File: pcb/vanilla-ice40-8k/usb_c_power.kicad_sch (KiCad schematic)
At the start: 25 parts, among them J8 Conn_01x02_Pin, U5 TPS563252DRLR, U6 TPS563252DRLR

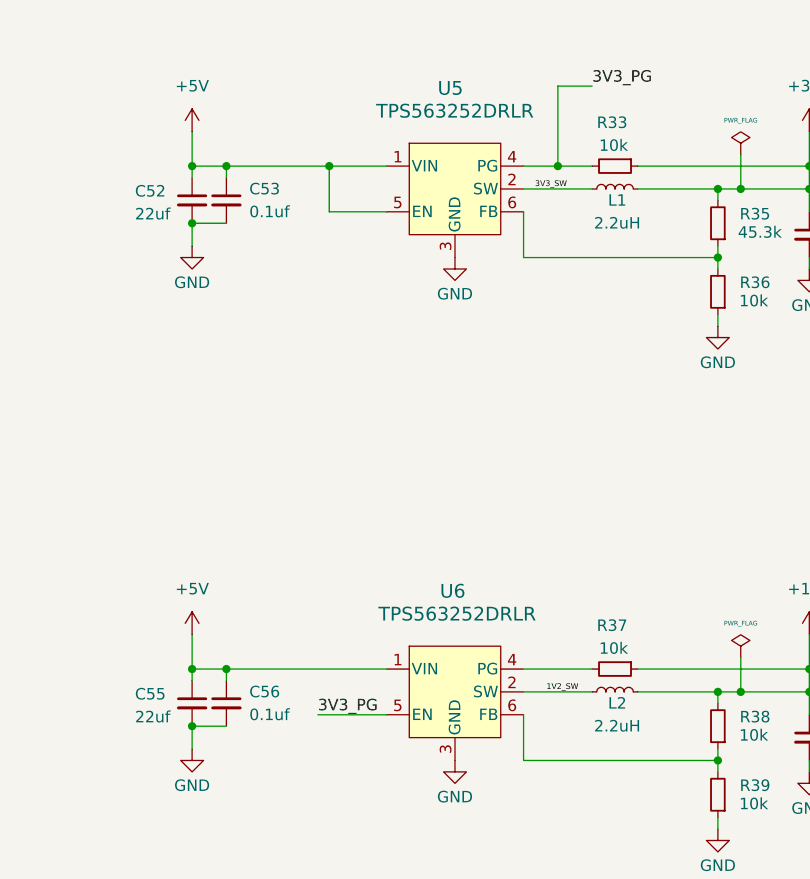
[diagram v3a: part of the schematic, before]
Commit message: [hx8k][pcb] rough layout of full board
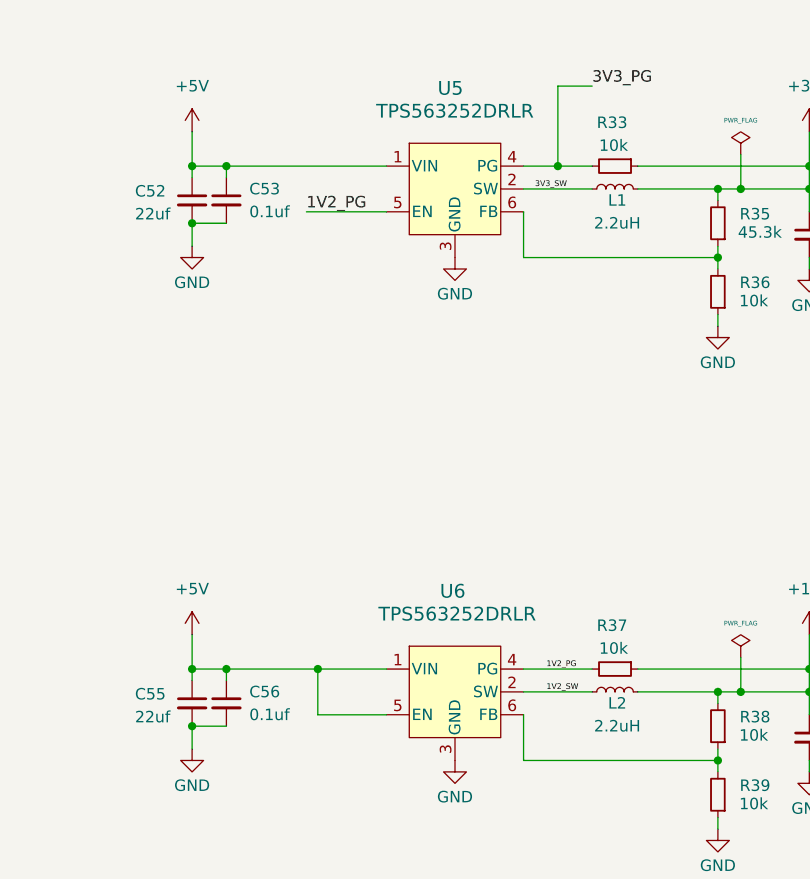
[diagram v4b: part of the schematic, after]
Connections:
- net +5V: now also U6.5 (EN); no longer U5.5 (EN)
- net 3V3_PG: no longer U6.5 (EN)
- net 1V2_PG: now reaches R37.2, U6.4 (PG)
- net 1V2_PG: now also U5.5 (EN)
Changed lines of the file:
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@@
-	)
-	(junction
-		(at 139.7 67.31)
-		(diameter 0)
-		(color 0 0 0 0)
 	)
 	(junction
@@
 	(junction
 		(at 124.46 67.31)
+		(diameter 0)
+		(color 0 0 0 0)
+	)
+	(junction
+		(at 138.43 123.19)
 		(diameter 0)
 		(color 0 0 0 0)
@@
 	(wire
 		(pts
-			(xy 139.7 67.31) (xy 139.7 72.39)
-		)
-		(stroke
-			(width 0)
-			(type default)
-		)
-	)
-	(wire
-		(pts
 			(xy 124.46 129.54) (xy 124.46 132.08)
 		)
@@
 	(wire
 		(pts
-			(xy 128.27 123.19) (xy 146.05 123.19)
+			(xy 128.27 123.19) (xy 138.43 123.19)
 		)
 		(stroke
@@
 	(wire
 		(pts
-			(xy 128.27 67.31) (xy 139.7 67.31)
+			(xy 128.27 67.31) (xy 146.05 67.31)
 		)
 		(stroke
@@
 	(wire
 		(pts
-			(xy 139.7 67.31) (xy 146.05 67.31)
-		)
-		(stroke
-			(width 0)
-			(type default)
-		)
-	)
-	(wire
-		(pts
 			(xy 43.18 31.75) (xy 43.18 34.29)
 		)
@@
 	(wire
 		(pts
+			(xy 138.43 123.19) (xy 146.05 123.19)
+		)
+		(stroke
+			(width 0)
+			(type default)
+		)
+	)
+	(wire
+		(pts
 			(xy 165.1 67.31) (xy 165.1 58.42)
 		)
@@
 	(wire
 		(pts
+			(xy 138.43 123.19) (xy 138.43 128.27)
+		)
+		(stroke
+			(width 0)
+			(type default)
+		)
+	)
+	(wire
+		(pts
 			(xy 182.88 69.85) (xy 185.42 69.85)
 		)
@@
 	(wire
 		(pts
-			(xy 139.7 72.39) (xy 146.05 72.39)
+			(xy 137.16 72.39) (xy 146.05 72.39)
 		)
 		(stroke
@@
 		)
 	)
-	(label "3V3_PG"
-		(at 138.43 128.27 0)
-		(effects
-			(font
-				(size 1.27 1.27)
-			)
-			(justify left bottom)
-		)
-	)
 	(label "USB_DN"
 		(at 60.96 81.28 0)
@@
 			(font
 				(size 0.635 0.635)
+			)
+			(justify left bottom)
+		)
+	)
+	(label "1V2_PG"
+		(at 163.83 123.19 0)
+		(effects
+			(font
+				(size 0.635 0.635)
+			)
+			(justify left bottom)
+		)
+	)
+	(label "1V2_PG"
+		(at 137.16 72.39 0)
+		(effects
+			(font
+				(size 1.27 1.27)
 			)
 			(justify left bottom)
@@
 		(polyline
 			(pts
-				(xy 111.76 50.8) (xy 111.76 93.98) (xy 220.98 93.98) (xy 220.98 50.8)
+				(xy 111.76 104.14) (xy 111.76 147.32) (xy 220.98 147.32) (xy 220.98 104.14)
 			)
 			(stroke
@@
 		(polyline
 			(pts
-				(xy 111.76 104.14) (xy 111.76 147.32) (xy 220.98 147.32) (xy 220.98 104.14)
+				(xy 111.76 50.8) (xy 111.76 93.98) (xy 220.98 93.98) (xy 220.98 50.8)
 			)
 			(stroke

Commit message: [hx8k][pcb] rough layout improvements
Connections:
- net USB_5V is gone; now on net +5V: FB3.2
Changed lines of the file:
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@@
 		(polyline
 			(pts
-				(xy 111.76 104.14) (xy 111.76 147.32) (xy 220.98 147.32) (xy 220.98 104.14)
+				(xy 111.76 50.8) (xy 111.76 93.98) (xy 220.98 93.98) (xy 220.98 50.8)
 			)
 			(stroke
@@
 		(polyline
 			(pts
-				(xy 111.76 50.8) (xy 111.76 93.98) (xy 220.98 93.98) (xy 220.98 50.8)
+				(xy 111.76 104.14) (xy 111.76 147.32) (xy 220.98 147.32) (xy 220.98 104.14)
 			)
 			(stroke
@@
 	(symbol
 		(lib_id "power:VBUS")
+		(at 72.39 58.42 0)
+		(unit 1)
+		(exclude_from_sim no)
+		(in_bom yes)
+		(on_board yes)
+		(dnp no)
+		(property "Reference" "#PWR094"
+			(at 72.39 62.23 0)
+			(effects
+				(font
+					(size 1.27 1.27)
+				)
+				(hide yes)
+			)
+		)
+		(property "Value" "+5V"
+			(at 72.39 53.34 0)
+			(effects
+				(font
+					(size 1.27 1.27)
+				)
+			)
+		)
+		(property "Footprint" ""
+			(at 72.39 58.42 0)
+			(effects
+				(font
+					(size 1.27 1.27)
+				)
+				(hide yes)
+			)
+		)
+		(property "Datasheet" ""
+			(at 72.39 58.42 0)
+			(effects
+				(font
+					(size 1.27 1.27)
+				)
+				(hide yes)
+			)
+		)
+		(property "Description" "Power symbol creates a global label with name \"VBUS\""
+			(at 72.39 58.42 0)
+			(effects
+				(font
+					(size 1.27 1.27)
+				)
+				(hide yes)
+			)
+		)
+		(pin "1"
+		)
+		(instances
+			(project "vanilla-ice40-8k"
+				(path "/6fdfbf4b-014a-4077-8dc3-7ce5ecaf5fe5/4c09157d-3537-4cf3-bc9c-21379ec730e4"
+					(reference "#PWR094")
+					(unit 1)
+				)
+			)
+		)
+	)
+	(symbol
+		(lib_id "power:VBUS")
 		(at 124.46 63.5 0)
 		(unit 1)
@@
 					(unit 1)
 				)
-			)
-		)
-	)
-	(symbol
-		(lib_id "power:VBUS")
-		(at 72.39 58.42 0)
-		(unit 1)
-		(exclude_from_sim no)
-		(in_bom yes)
-		(on_board yes)
-		(dnp no)
-		(property "Reference" "#PWR075"
-			(at 72.39 62.23 0)
-			(effects
-				(font
-					(size 1.27 1.27)
-				)
-				(hide yes)
-			)
-		)
-		(property "Value" "USB_5V"
-			(at 72.644 54.61 0)
-			(effects
-				(font
-					(size 1.27 1.27)
-				)
-			)
-		)
-		(property "Footprint" ""
-			(at 72.39 58.42 0)
-			(effects
-				(font
-					(size 1.27 1.27)
-				)
-				(hide yes)
-			)
-		)
-		(property "Datasheet" ""
-			(at 72.39 58.42 0)
-			(effects
-				(font
-					(size 1.27 1.27)
-				)
-				(hide yes)
-			)
-		)
-		(property "Description" "Power symbol creates a global label with name \"VBUS\""
-			(at 72.39 58.42 0)
-			(effects
-				(font
-					(size 1.27 1.27)
-				)
-				(hide yes)
-			)
-		)
-		(pin "1"
-		)
-		(instances
-			(project "vanilla-ice40-8k"
-				(path "/6fdfbf4b-014a-4077-8dc3-7ce5ecaf5fe5/4c09157d-3537-4cf3-bc9c-21379ec730e4"
-					(reference "#PWR075")
-					(unit 1)
-				)

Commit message: [hx8k][pcb] move top level to use symbol lib
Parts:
- C51, C53, C56, C58, C59: symbol Device:C_Small -> !Misc:C_0.1uf_0402
- R31, R32, R34, R35: symbol Device:R_Small -> !Misc:R_2.2K_0603
- R33, R36, R37, R38, R39: symbol Device:R_Small -> !Misc:R_10K_0603

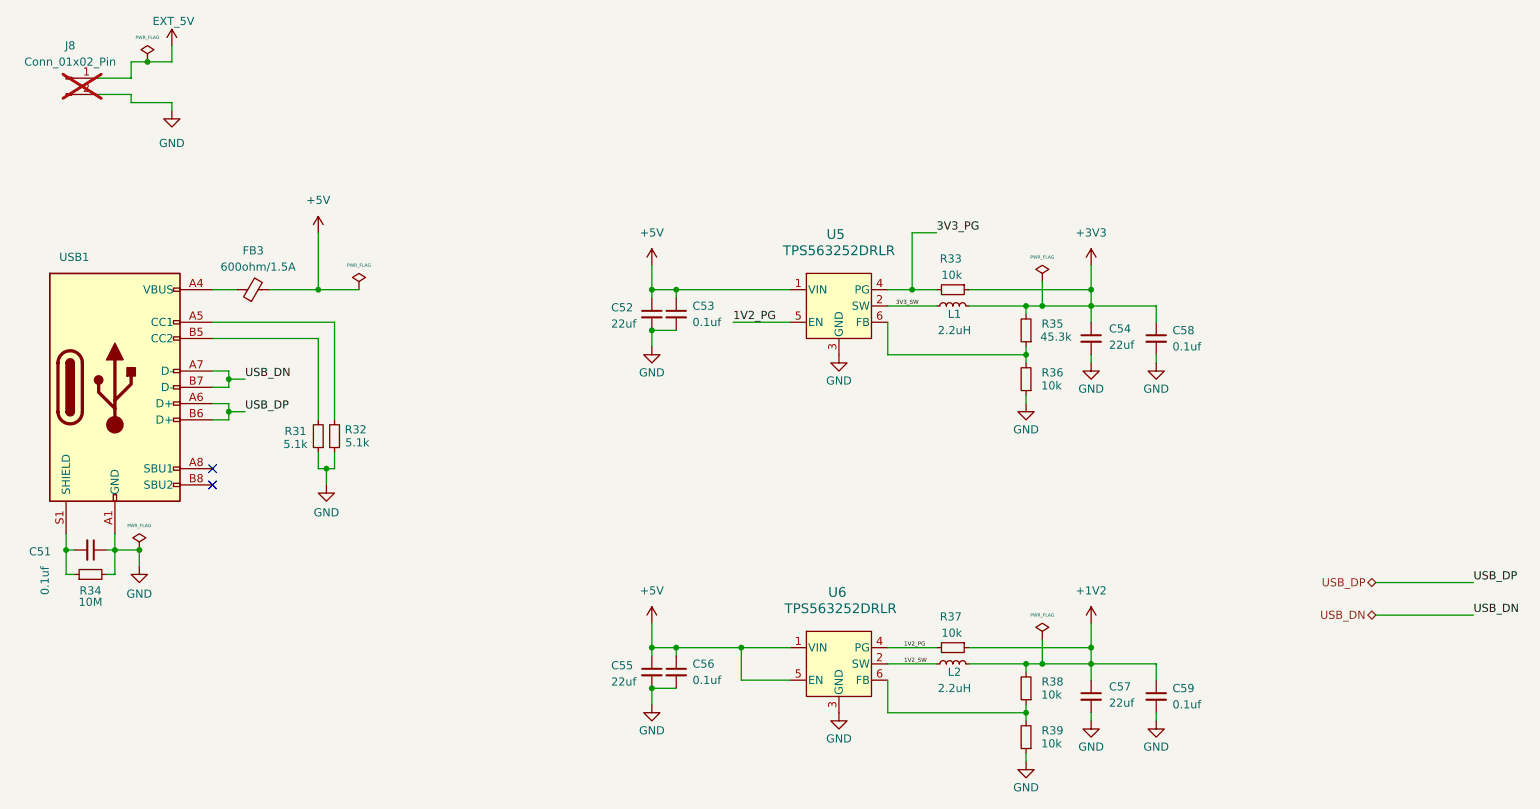
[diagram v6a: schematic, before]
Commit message: [hx8k][pcb] move usb_c_power to use symbol lib
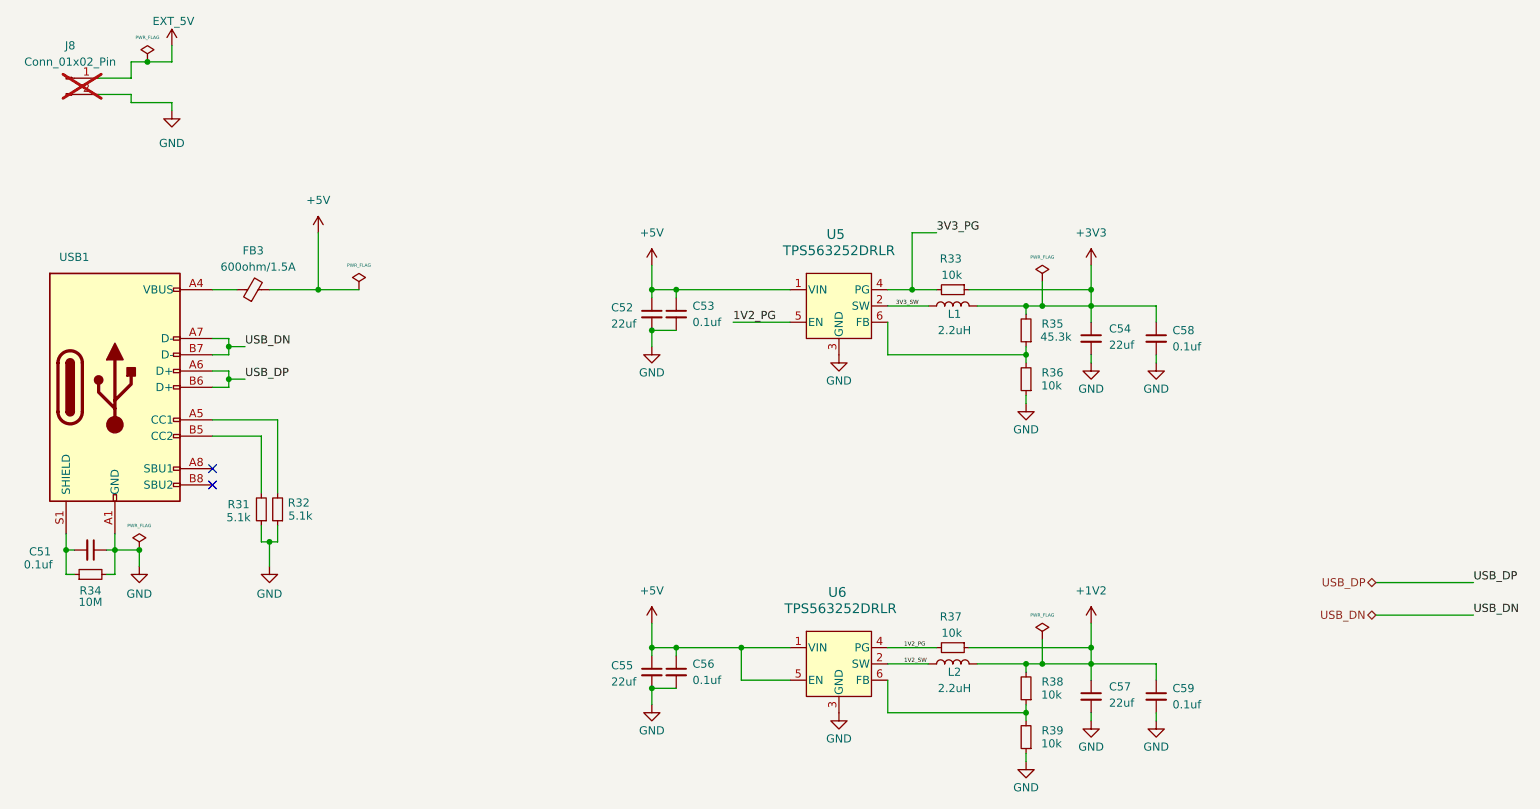
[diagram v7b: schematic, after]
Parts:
- C52, C54, C55, C57: symbol Device:C_Small -> !Misc:C_22uf_0603; LCSC Part # C59461 -> C59461
- FB3: footprint Inductor_SMD:L_0603_1608Metric -> Inductor_SMD:L_0805_2012Metric; symbol Device:FerriteBead_Small -> !Misc:FB_600; Digi-Key Part Number 490-5258-1-ND -> 240-2399-1-ND; LCSC Part # C1002 -> C1017
- L1, L2: symbol Device:L_Small -> !Misc:L_2.2uh_3A; Digi-Key Part Number 490-10649-1-ND -> 490-13055-1-ND; LCSC Part # C391305 -> C576403
- R31, R32: symbol !Misc:R_2.2K_0603 -> !Misc:R_5.1K_0603
- R34: symbol !Misc:R_2.2K_0603 -> !Misc:R_10M_0603
- U5, U6: footprint TPS563252DRLR:SOT6_DRL_TEX -> !Misc:SOT6_DRL_TEX; symbol TPS563252DRLR:TPS563252DRLR -> !Misc:TPS563257DRLR; Digi-Key Part Number 296-TPS563252DRLRCT-ND -> 296-TPS563257DRLRCT-ND; LCSC Part # C19188399 -> C20539656
- USB1: footprint Connector_USB:USB_C_Receptacle_GCT_USB4105-xx-A_16P_TopMnt_Horizontal -> !Misc:USB_C_Receptacle_GCT_USB4105-xx-A_16P_TopMnt_Horizontal; symbol Connector:USB_C_Receptacle_USB2.0_16P -> !Misc:USB_C_Receptacle_USB2.0_16P
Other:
- moved on the sheet: R31, R32

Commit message: [hx8k][pcb] move programmer to symbol lib
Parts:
- FB3: footprint Inductor_SMD:L_0805_2012Metric -> Inductor_SMD:L_1206_3216Metric; symbol !Misc:FB_600 -> !Misc:FB_600_1206; Digi-Key Part Number 240-2399-1-ND -> 490-1057-1-ND; LCSC Part # C1017 -> C16902
- R35: symbol !Misc:R_2.2K_0603 -> !Misc:R_45.3K_0603
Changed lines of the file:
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@@
 	)
 	(symbol
-		(lib_id "!Misc:R_2.2K_0603")
+		(lib_id "!Misc:R_45.3K_0603")
 		(at 182.88 73.66 180)
 		(unit 1)
@@
 			)
 		)
-		(property "Description" "Resistor, small symbol"
+		(property "Description" "45.3K 0603 Resistor"
 			(at 182.88 73.66 0)
 			(effects
@@
 	)
 	(symbol
-		(lib_id "!Misc:FB_600")
+		(lib_id "!Misc:FB_600_1206")
 		(at 62.23 67.31 90)
 		(unit 1)
@@
 			)
 		)
-		(property "Footprint" "Inductor_SMD:L_0805_2012Metric"
+		(property "Footprint" "Inductor_SMD:L_1206_3216Metric"
 			(at 62.23 69.088 90)
 			(effects
@@
 			)
 		)
-		(property "Description" "Ferrite bead, 600ohm, 0805"
-			(at 62.23 67.31 0)
-			(effects
-				(font
-					(size 1.27 1.27)
-				)
-				(hide yes)
-			)
-		)
-		(property "LCSC Part #" "C1017"
+		(property "Description" "Ferrite bead, 600ohm, 1206 1.5A"
+			(at 62.23 67.31 0)
+			(effects
+				(font
+					(size 1.27 1.27)
+				)
+				(hide yes)
+			)
+		)
+		(property "LCSC Part #" "C16902"
 			(at 62.23 67.31 0)
 			(effects
@@
 			)
 		)
-		(property "Digi-Key Part Number" "240-2399-1-ND"
-			(at 62.23 67.31 0)
-			(effects
+		(property "Digi-Key Part Number" "490-1057-1-ND"
+			(at 62.23 67.31 0)
+			(effects
